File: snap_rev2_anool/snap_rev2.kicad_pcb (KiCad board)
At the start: 2 copper layers, 60 x 22 mm, 29 parts, among them J1 SJ2-35863B1, P1 CONN_02X05, Q1 TSM2301, SW1 1825910-6, U1 TPS610986, U2 MDBT42Q, Y1 32786Hz

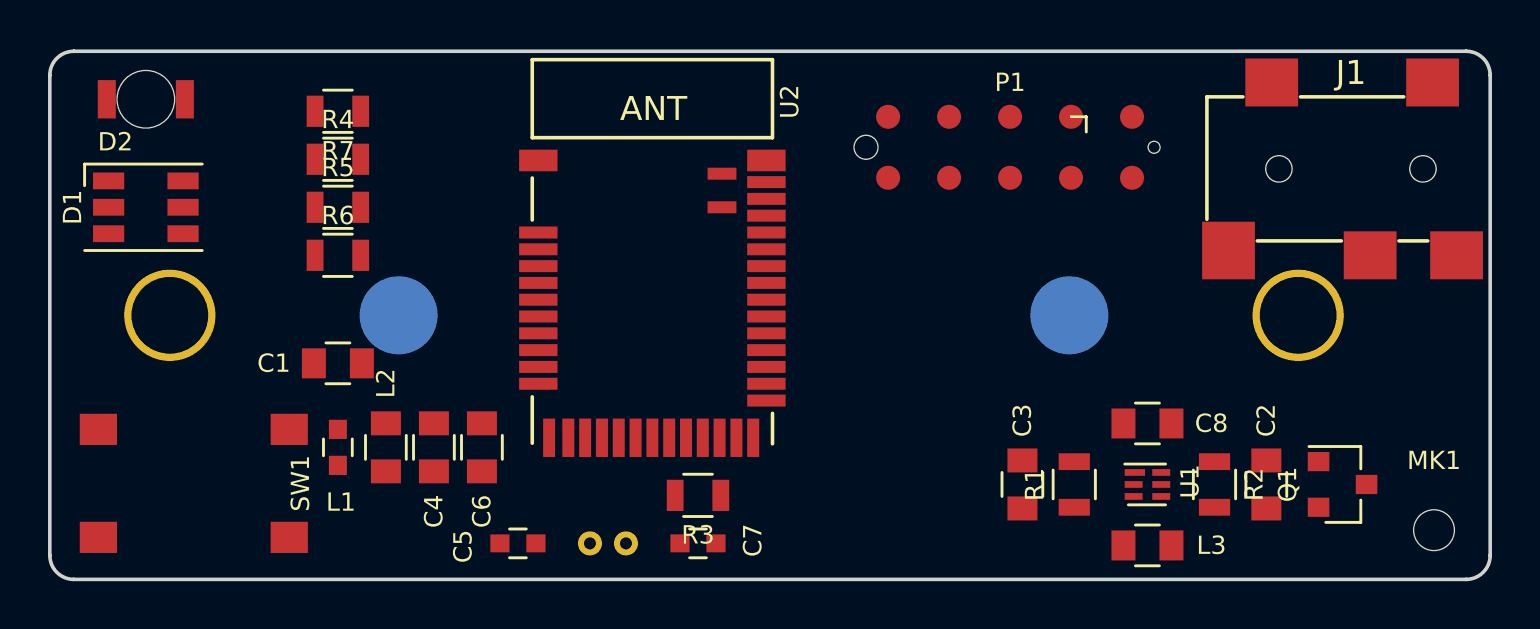
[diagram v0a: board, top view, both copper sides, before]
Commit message: camera trigger anool version2
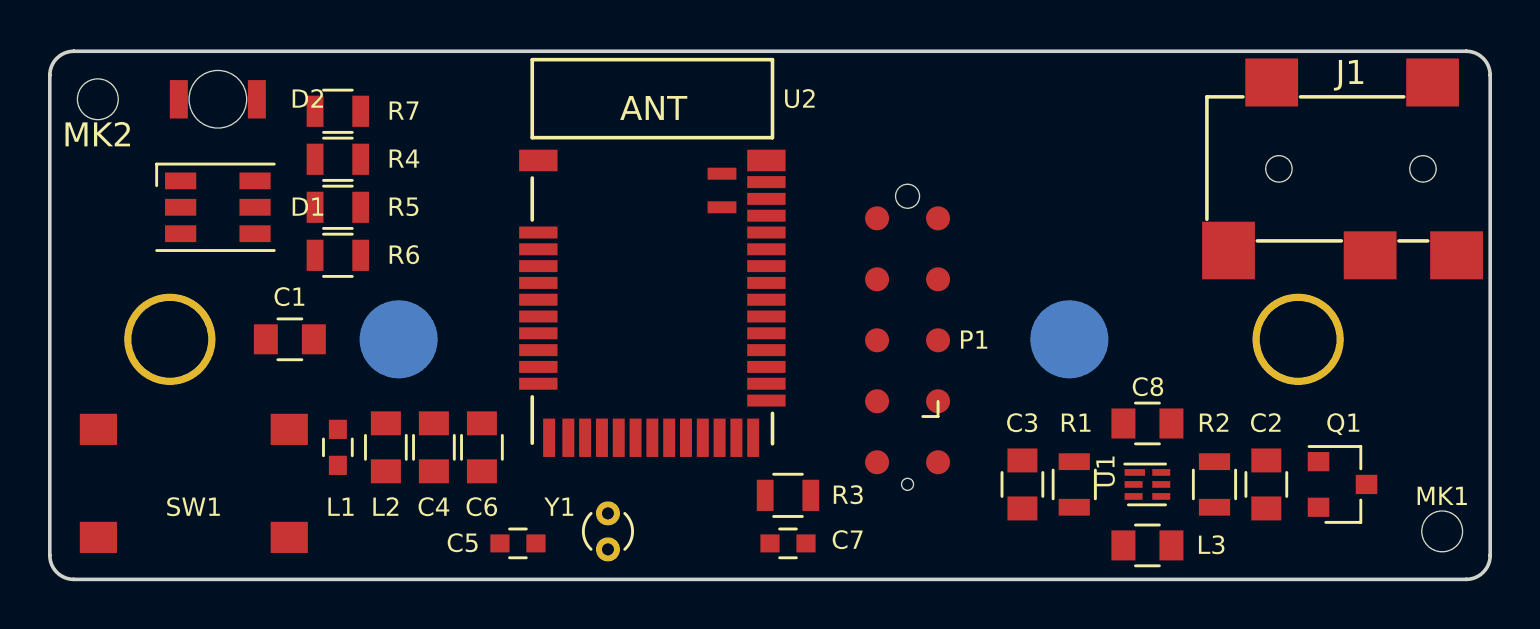
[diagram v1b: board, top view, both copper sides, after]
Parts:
- added MK2: Mounting_Hole_PAD, snap_fp:MountingHole_1.7mm_M1.6, F.Cu at (52.0, 90.0)
- Y1: moved to F.Cu
- moved P1 9.10 mm to (85.7, 100.0), turned to 90 degrees
- moved C7 3.75 mm to (80.8, 108.5)
- moved R3 3.75 mm to (80.8, 106.5)
- moved D1 3.00 mm to (57.0, 94.5)
- moved D2 3.00 mm to (57.0, 90.0)
- moved C1 2.24 mm to (60.0, 100.0)
- moved Y1 1.46 mm to (73.2, 107.2), turned to 270 degrees
- moved BT1 1.00 mm to (78.5, 100.0)
- moved MK1 0.34 mm to (108.0, 108.0)
